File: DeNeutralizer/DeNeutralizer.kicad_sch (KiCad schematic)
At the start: 20 parts, among them J1 Screw_Terminal_01x03, J2 Screw_Terminal_01x03, J3 Screw_Terminal_01x03, J4 Screw_Terminal_01x03, J5 Screw_Terminal_01x02, J6 Screw_Terminal_01x05, J7 Screw_Terminal_01x02, U1 PC817

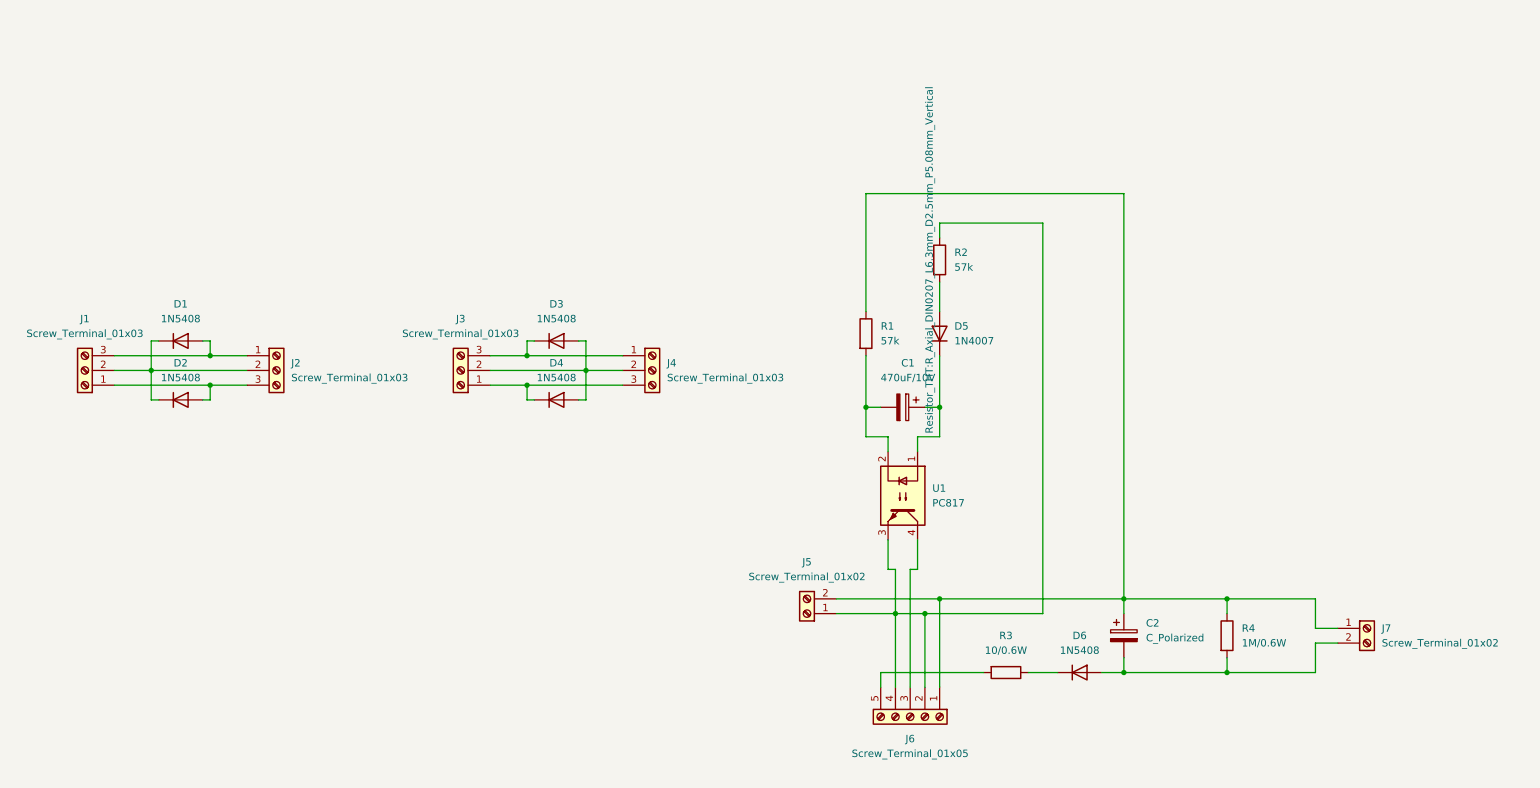
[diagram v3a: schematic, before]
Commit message: Add jumper and for switcihing between modes and crt for external ripple capacitor
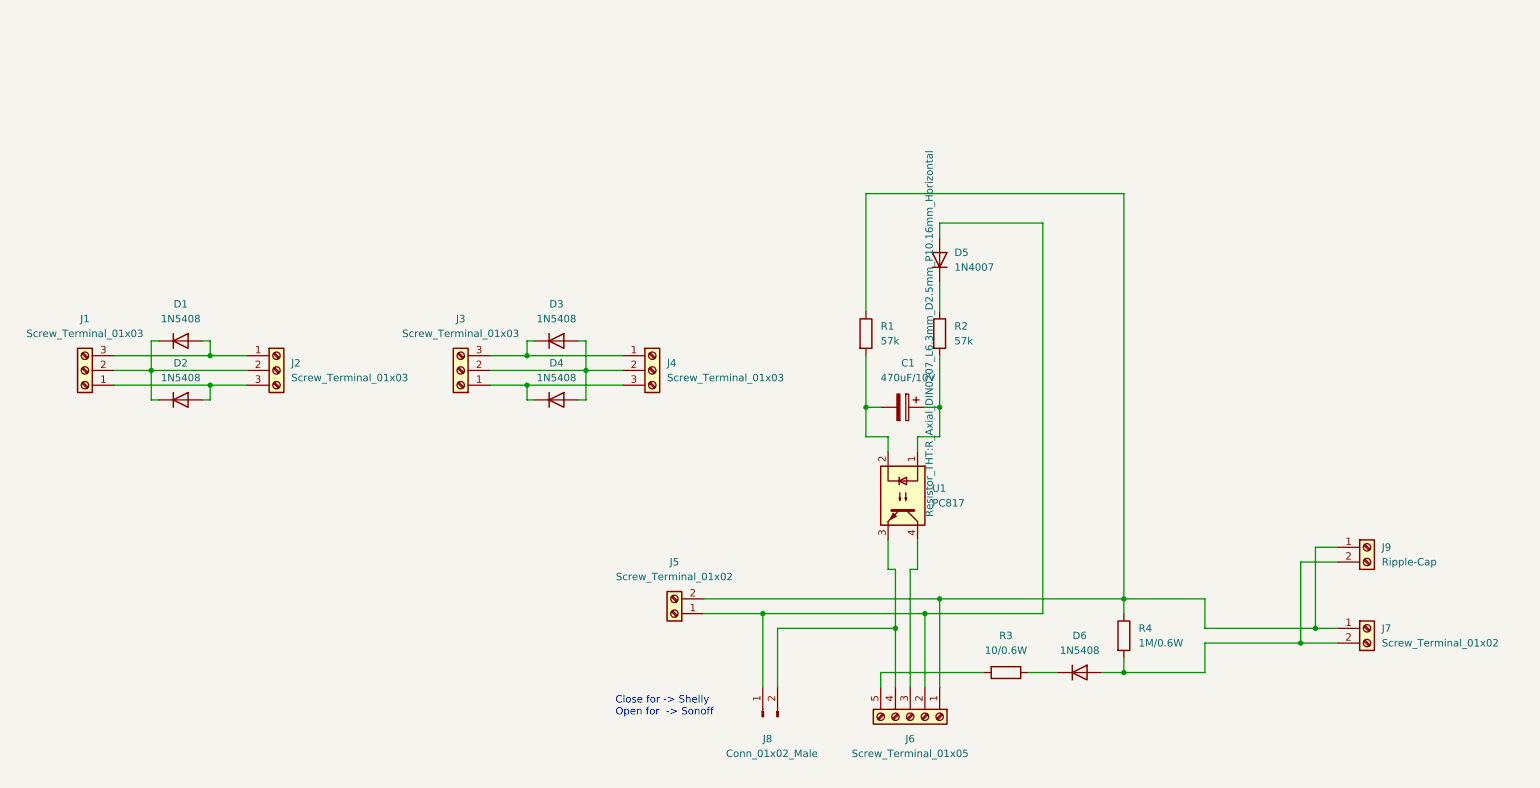
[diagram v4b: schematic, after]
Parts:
- removed C2: C_Polarized, Capacitor_THT:CP_Radial_D8.0mm_P5.00mm, symbol Device:C_Polarized
- added J8: Conn_01x02_Male, Connector_PinHeader_2.54mm:PinHeader_1x02_P2.54mm_Vertical, symbol Connector:Conn_01x02_Male
- added J9: Ripple-Cap, TerminalBlock:TerminalBlock_bornier-2_P5.08mm, symbol Connector:Screw_Terminal_01x02
- D5: footprint Diode_THT:D_DO-41_SOD81_P5.08mm_Vertical_AnodeUp -> Diode_THT:D_DO-41_SOD81_P10.16mm_Horizontal
- R2: footprint Resistor_THT:R_Axial_DIN0207_L6.3mm_D2.5mm_P5.08mm_Vertical -> Resistor_THT:R_Axial_DIN0207_L6.3mm_D2.5mm_P10.16mm_Horizontal
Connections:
- net at J5.2 (Pin_2), J6.1 (Pin_1), J7.1 (Pin_1)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: now also J9.1 (Pin_1)
- net at C1.1, U1.1: now also R2.2; no longer D5.1 (K)
- net at D5.2 (A): now also J5.1 (Pin_1), J6.2 (Pin_2), J8.1 (Pin_1); no longer R2.2
- net at D6.2 (A), J7.2 (Pin_2), R4.2: now also J9.2 (Pin_2)
- new net: J6.4 (Pin_4), J8.2 (Pin_2), U1.3
- new net: D5.1 (K), R2.1
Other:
- note added: "Close for -> Shelly Open for -> Sonoff"
- moved on the sheet: D5, J5, R2, R4

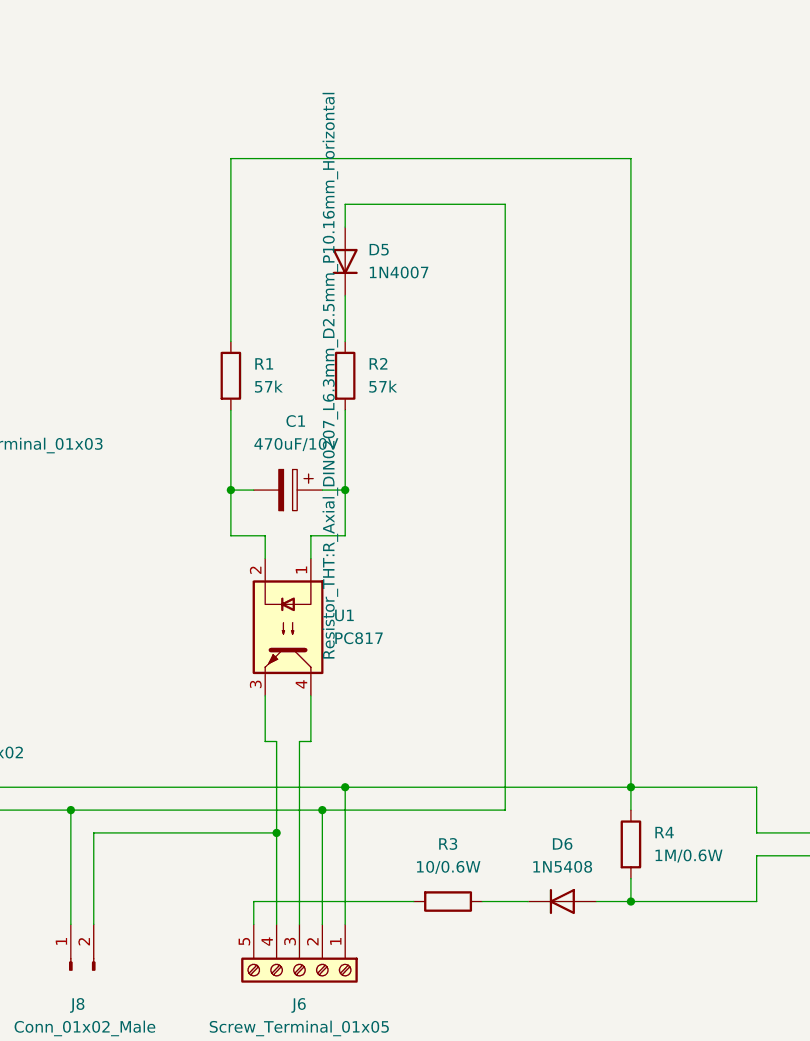
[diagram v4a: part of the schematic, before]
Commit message: Add 5W resistor insted 0.6W for serial protection
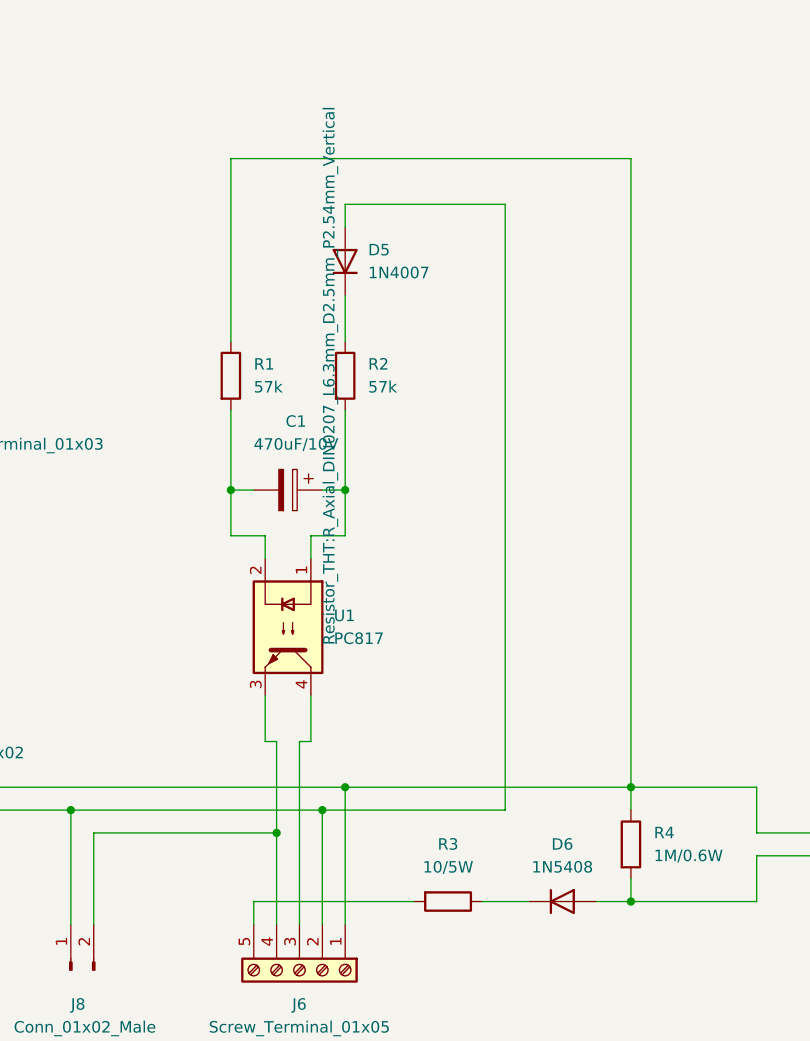
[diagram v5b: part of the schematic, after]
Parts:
- D5: footprint Diode_THT:D_DO-41_SOD81_P10.16mm_Horizontal -> Diode_THT:D_DO-41_SOD81_P2.54mm_Vertical_KathodeUp
- R1, R2: footprint Resistor_THT:R_Axial_DIN0207_L6.3mm_D2.5mm_P10.16mm_Horizontal -> Resistor_THT:R_Axial_DIN0207_L6.3mm_D2.5mm_P2.54mm_Vertical
- R3: value 10/0.6W -> 10/5W; footprint Resistor_THT:R_Axial_DIN0414_L11.9mm_D4.5mm_P5.08mm_Vertical -> Resistor_THT:R_Axial_Power_L25.0mm_W9.0mm_P27.94mm
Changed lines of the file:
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@@
     (in_bom yes) (on_board yes) (fields_autoplaced)
     (property "Reference" "R3" (id 0) (at 194.31 132.08 90))
-    (property "Value" "10/0.6W" (id 1) (at 194.31 134.62 90))
-    (property "Footprint" "Resistor_THT:R_Axial_DIN0414_L11.9mm_D4.5mm_P5.08mm_Vertical" (id 2) (at 194.31 136.652 90)
+    (property "Value" "10/5W" (id 1) (at 194.31 134.62 90))
+    (property "Footprint" "Resistor_THT:R_Axial_Power_L25.0mm_W9.0mm_P27.94mm" (id 2) (at 194.31 136.652 90)
       (effects (font (size 1.27 1.27)) hide)
     )
@@
       (effects (font (size 1.27 1.27)) (justify right))
     )
-    (property "Footprint" "Diode_THT:D_DO-41_SOD81_P10.16mm_Horizontal" (id 2) (at 187.325 67.31 0)
+    (property "Footprint" "Diode_THT:D_DO-41_SOD81_P2.54mm_Vertical_KathodeUp" (id 2) (at 187.325 67.31 0)
       (effects (font (size 1.27 1.27)) hide)
     )
@@
       (effects (font (size 1.27 1.27)) (justify left))
     )
-    (property "Footprint" "Resistor_THT:R_Axial_DIN0207_L6.3mm_D2.5mm_P10.16mm_Horizontal" (id 2) (at 181.102 80.01 90))
+    (property "Footprint" "Resistor_THT:R_Axial_DIN0207_L6.3mm_D2.5mm_P2.54mm_Vertical" (id 2) (at 181.102 80.01 90))
     (property "Datasheet" "~" (id 3) (at 182.88 80.01 0)
       (effects (font (size 1.27 1.27)) hide)
@@
       (effects (font (size 1.27 1.27)) (justify left))
     )
-    (property "Footprint" "Resistor_THT:R_Axial_DIN0207_L6.3mm_D2.5mm_P10.16mm_Horizontal" (id 2) (at 168.402 80.01 90)
+    (property "Footprint" "Resistor_THT:R_Axial_DIN0207_L6.3mm_D2.5mm_P2.54mm_Vertical" (id 2) (at 168.402 80.01 90)
       (effects (font (size 1.27 1.27)) hide)
     )
@@
     )
     (path "/73c07c85-8041-4fbe-ab32-e3c9c0c750ce"
-      (reference "D5") (unit 1) (value "1N4007") (footprint "Diode_THT:D_DO-41_SOD81_P10.16mm_Horizontal")
+      (reference "D5") (unit 1) (value "1N4007") (footprint "Diode_THT:D_DO-41_SOD81_P2.54mm_Vertical_KathodeUp")
     )
     (path "/86ae69c9-3834-40ff-9cb9-8d2dfc8c1cb2"
@@
     )
     (path "/f07b8ebe-0dd1-4e28-a031-b29c3a87e7a8"
-      (reference "R1") (unit 1) (value "57k") (footprint "Resistor_THT:R_Axial_DIN0207_L6.3mm_D2.5mm_P10.16mm_Horizontal")
+      (reference "R1") (unit 1) (value "57k") (footprint "Resistor_THT:R_Axial_DIN0207_L6.3mm_D2.5mm_P2.54mm_Vertical")
     )
     (path "/7b657e58-9581-4cba-99a8-54085112bee6"
-      (reference "R2") (unit 1) (value "57k") (footprint "Resistor_THT:R_Axial_DIN0207_L6.3mm_D2.5mm_P10.16mm_Horizontal")
+      (reference "R2") (unit 1) (value "57k") (footprint "Resistor_THT:R_Axial_DIN0207_L6.3mm_D2.5mm_P2.54mm_Vertical")
     )
     (path "/4188abe1-a17a-452b-82c2-c4cbdecdd572"
-      (reference "R3") (unit 1) (value "10/0.6W") (footprint "Resistor_THT:R_Axial_DIN0414_L11.9mm_D4.5mm_P5.08mm_Vertical")
+      (reference "R3") (unit 1) (value "10/5W") (footprint "Resistor_THT:R_Axial_Power_L25.0mm_W9.0mm_P27.94mm")
     )
     (path "/834dcae7-39c3-4120-97e3-78b7973f4ba7"

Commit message: Make tha board as low profile as it can for this time :D
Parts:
- D6: footprint Diode_THT:D_DO-201AD_P5.08mm_Vertical_KathodeUp -> Diode_THT:D_DO-201AD_P12.70mm_Horizontal
- R4: footprint Resistor_THT:R_Axial_DIN0414_L11.9mm_D4.5mm_P5.08mm_Vertical -> Resistor_THT:R_Axial_DIN0207_L6.3mm_D2.5mm_P5.08mm_Vertical

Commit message: Add 3D model of the Shelly
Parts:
- added F1: Fuse, symbol Device:Fuse
- added R5: 500k, Resistor_THT:R_Axial_DIN0207_L6.3mm_D2.5mm_P2.54mm_Vertical, symbol Device:R
- J5: value Screw_Terminal_01x02 -> Power
- J7: value Screw_Terminal_01x02 -> Load
- R3: value 10/5W -> 5/5W
- R4: value 1M/0.6W -> 500k; footprint Resistor_THT:R_Axial_DIN0207_L6.3mm_D2.5mm_P5.08mm_Vertical -> Resistor_THT:R_Axial_DIN0207_L6.3mm_D2.5mm_P2.54mm_Vertical
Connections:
- net at J5.2 (Pin_2), J6.1 (Pin_1), J7.1 (Pin_1)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: now also R4.2; no longer R4.1
- net at R3.1: now also F1.1; no longer D6.1 (K)
- net at D6.2 (A), J7.2 (Pin_2), J9.2 (Pin_2): now also R5.1; no longer R4.2
- new net: D6.1 (K), F1.2
- new net: R4.1, R5.2
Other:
- moved on the sheet: D6, J6, J7, J9, R3, R4
